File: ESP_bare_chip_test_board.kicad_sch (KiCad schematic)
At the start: 0 parts

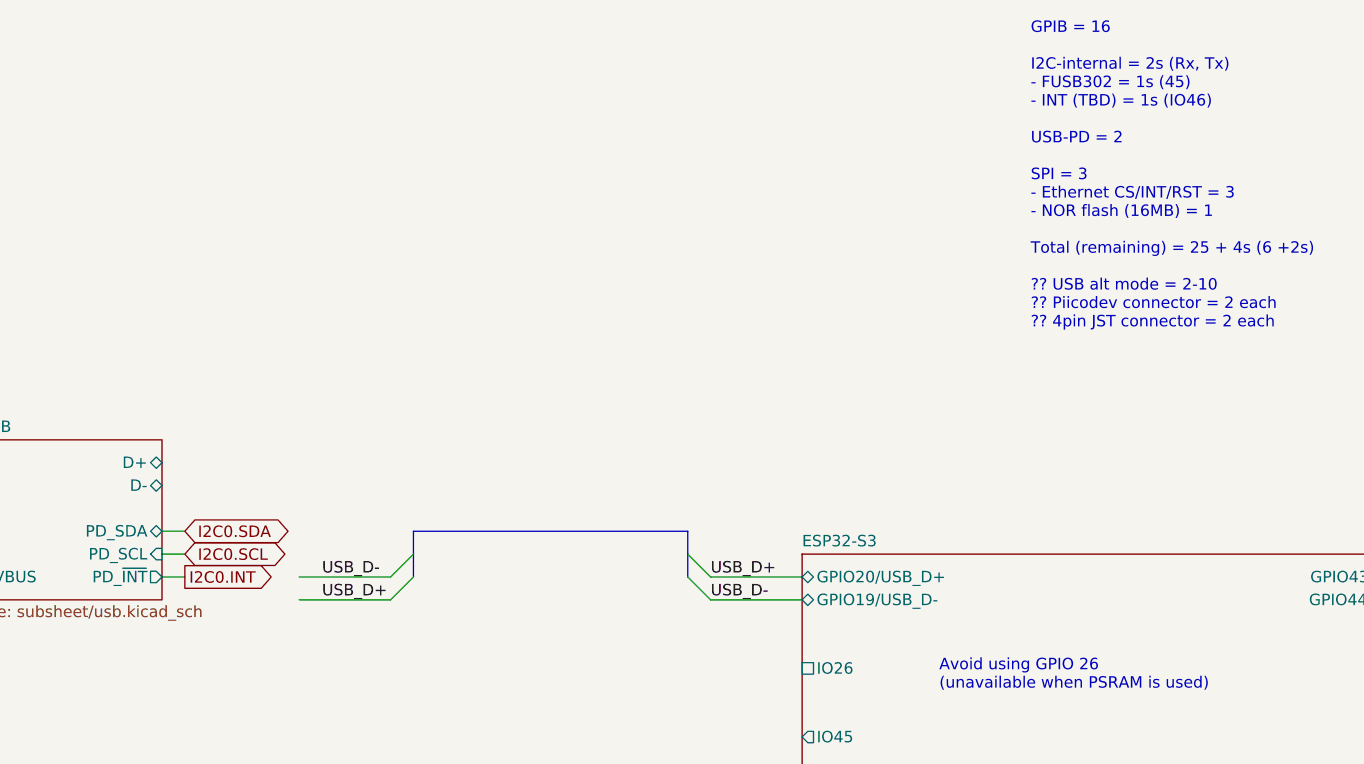
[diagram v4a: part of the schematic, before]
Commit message: Add barrel jack to schematic
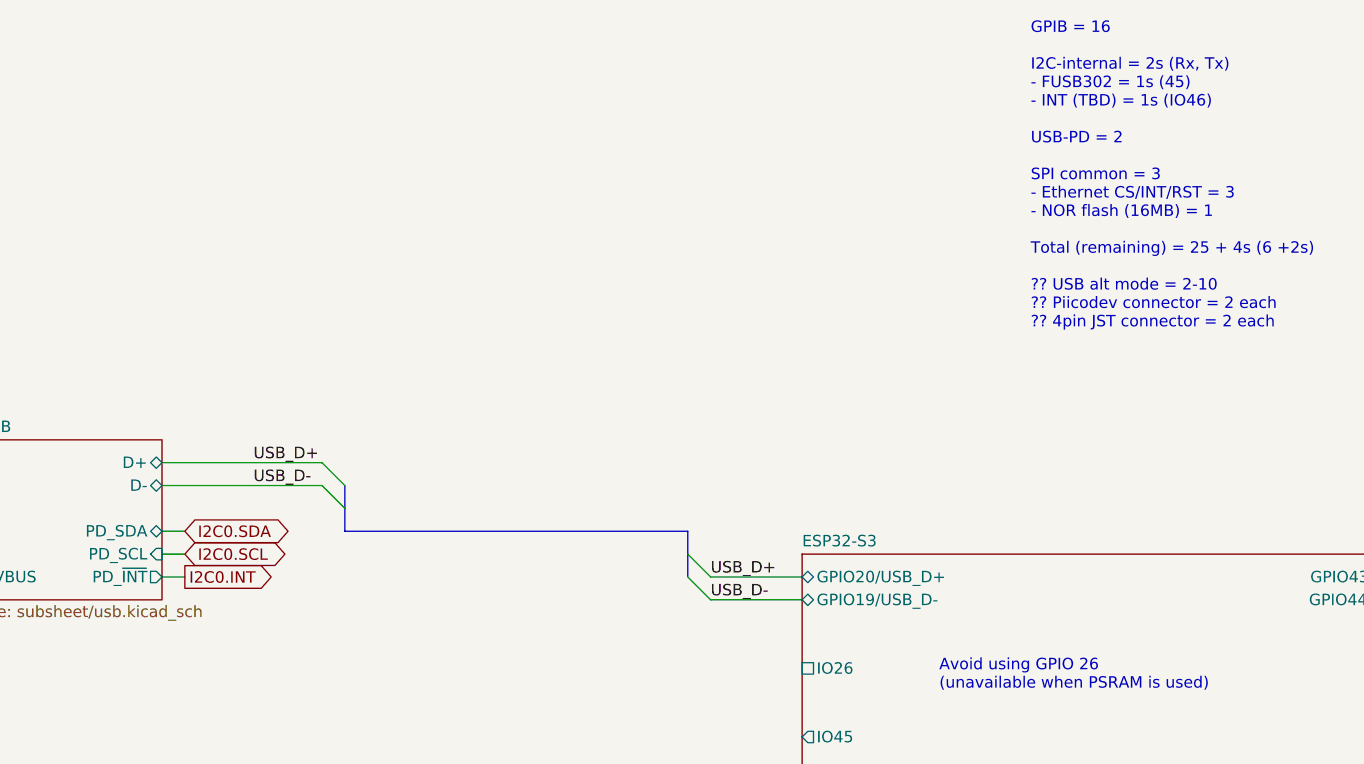
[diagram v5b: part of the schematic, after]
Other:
- note added: "~~ GPIO count ~~ Unrestricted = 31 Special = 6s (0, 45, 46, Tx, Rx) Unused if possible = 1u (26) GPIB = 16 I2C-internal = 2s (Rx, Tx) - FUSB302 = 1s (45) - INT (TBD) = 1s (IO46) USB-PD = 2 SPI common = 3 - Ethernet CS/INT/RST = 3 - NOR flash (16MB) = 1 Total (remaining) = 25 + 4s (6 +2s) ?? USB alt mode = 2-10 ?? Piicodev connector = 2 each ?? 4pin JST connector = 2 each"
- note removed: "~~ GPIO count ~~ Unrestricted = 31 Special = 6s (0, 45, 46, Tx, Rx) Unused if possible = 1u (26) GPIB = 16 I2C-internal = 2s (Rx, Tx) - FUSB302 = 1s (45) - INT (TBD) = 1s (IO46) USB-PD = 2 SPI = 3 - Ethernet CS/INT/RST = 3 - NOR flash (16MB) = 1 Total (remaining) = 25 + 4s (6 +2s) ?? USB alt mode = 2-10 ?? Piicodev connector = 2 each ?? 4pin JST connector = 2 each"
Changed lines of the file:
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@@
 	)
 	(bus_entry
-		(at 63.5 33.02)
-		(size 2.54 -2.54)
+		(at 55.88 22.86)
+		(size 2.54 2.54)
 		(stroke
 			(width 0)
@@
 	)
 	(bus_entry
-		(at 63.5 35.56)
-		(size 2.54 -2.54)
+		(at 55.88 20.32)
+		(size 2.54 2.54)
 		(stroke
 			(width 0)
@@
 	(wire
 		(pts
-			(xy 53.34 35.56) (xy 63.5 35.56)
-		)
-		(stroke
-			(width 0)
-			(type default)
-		)
-	)
-	(wire
-		(pts
 			(xy 17.78 33.02) (xy 15.24 33.02)
 		)
@@
 	(bus
 		(pts
-			(xy 66.04 30.48) (xy 66.04 27.94)
+			(xy 58.42 25.4) (xy 58.42 27.94)
 		)
 		(stroke
@@
 		)
 	)
+	(wire
+		(pts
+			(xy 38.1 22.86) (xy 55.88 22.86)
+		)
+		(stroke
+			(width 0)
+			(type default)
+		)
+	)
 	(bus
 		(pts
@@
 		)
 	)
+	(wire
+		(pts
+			(xy 88.9 91.44) (xy 88.9 121.92)
+		)
+		(stroke
+			(width 0)
+			(type default)
+		)
+	)
 	(bus
 		(pts
-			(xy 66.04 27.94) (xy 96.52 27.94)
-		)
-		(stroke
-			(width 0)
-			(type default)
-		)
-	)
-	(wire
-		(pts
-			(xy 88.9 91.44) (xy 88.9 121.92)
+			(xy 58.42 27.94) (xy 96.52 27.94)
 		)
 		(stroke
@@
 	(wire
 		(pts
+			(xy 38.1 20.32) (xy 55.88 20.32)
+		)
+		(stroke
+			(width 0)
+			(type default)
+		)
+	)
+	(wire
+		(pts
 			(xy 88.9 121.92) (xy 88.9 134.62)
 		)
@@
 	(wire
 		(pts
-			(xy 53.34 33.02) (xy 63.5 33.02)
-		)
-		(stroke
-			(width 0)
-			(type default)
-		)
-	)
-	(wire
-		(pts
 			(xy 99.06 35.56) (xy 109.22 35.56)
 		)
@@
 	(bus
 		(pts
-			(xy 66.04 33.02) (xy 66.04 30.48)
+			(xy 58.42 22.86) (xy 58.42 25.4)
 		)
 		(stroke
@@
 		)
 	)
-	(text "~~ GPIO count ~~\nUnrestricted = 31\nSpecial = 6s (0, 45, 46, Tx, Rx)\nUnused if possible = 1u (26)\n\nGPIB = 16\n\nI2C-internal = 2s (Rx, Tx)\n- FUSB302 = 1s (45)\n- INT (TBD) = 1s (IO46)\n\nUSB-PD = 2\n\nSPI = 3\n- Ethernet CS/INT/RST = 3\n- NOR flash (16MB) = 1\n\nTotal (remaining) = 25 + 4s (6 +2s)\n\n?? USB alt mode = 2-10\n?? Piicodev connector = 2 each\n?? 4pin JST connector = 2 each\n  "
+	(text "~~ GPIO count ~~\nUnrestricted = 31\nSpecial = 6s (0, 45, 46, Tx, Rx)\nUnused if possible = 1u (26)\n\nGPIB = 16\n\nI2C-internal = 2s (Rx, Tx)\n- FUSB302 = 1s (45)\n- INT (TBD) = 1s (IO46)\n\nUSB-PD = 2\n\nSPI common = 3\n- Ethernet CS/INT/RST = 3\n- NOR flash (16MB) = 1\n\nTotal (remaining) = 25 + 4s (6 +2s)\n\n?? USB alt mode = 2-10\n?? Piicodev connector = 2 each\n?? 4pin JST connector = 2 each\n  "
 		(exclude_from_sim no)
 		(at 134.62 7.62 0)
@@
 	)
 	(label "USB_D+"
-		(at 55.88 35.56 0)
+		(at 48.26 20.32 0)
 		(fields_autoplaced yes)
 		(effects
@@
 	)
 	(label "USB_D-"
-		(at 55.88 33.02 0)
-		(fields_autoplaced yes)
-		(effects
+		(at 48.26 22.86 0)
+		(fields_autoplaced yes)
+		(effects

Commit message: Uknown changes?File formats?
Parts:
- added R101: 0, Resistor_SMD:R_0402_1005Metric, symbol Device:R_US
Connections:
- net ESP32-C3/IO2/STRAP^{PU}: now also R101.2
- net ~{ETH_INT}: now also R101.1

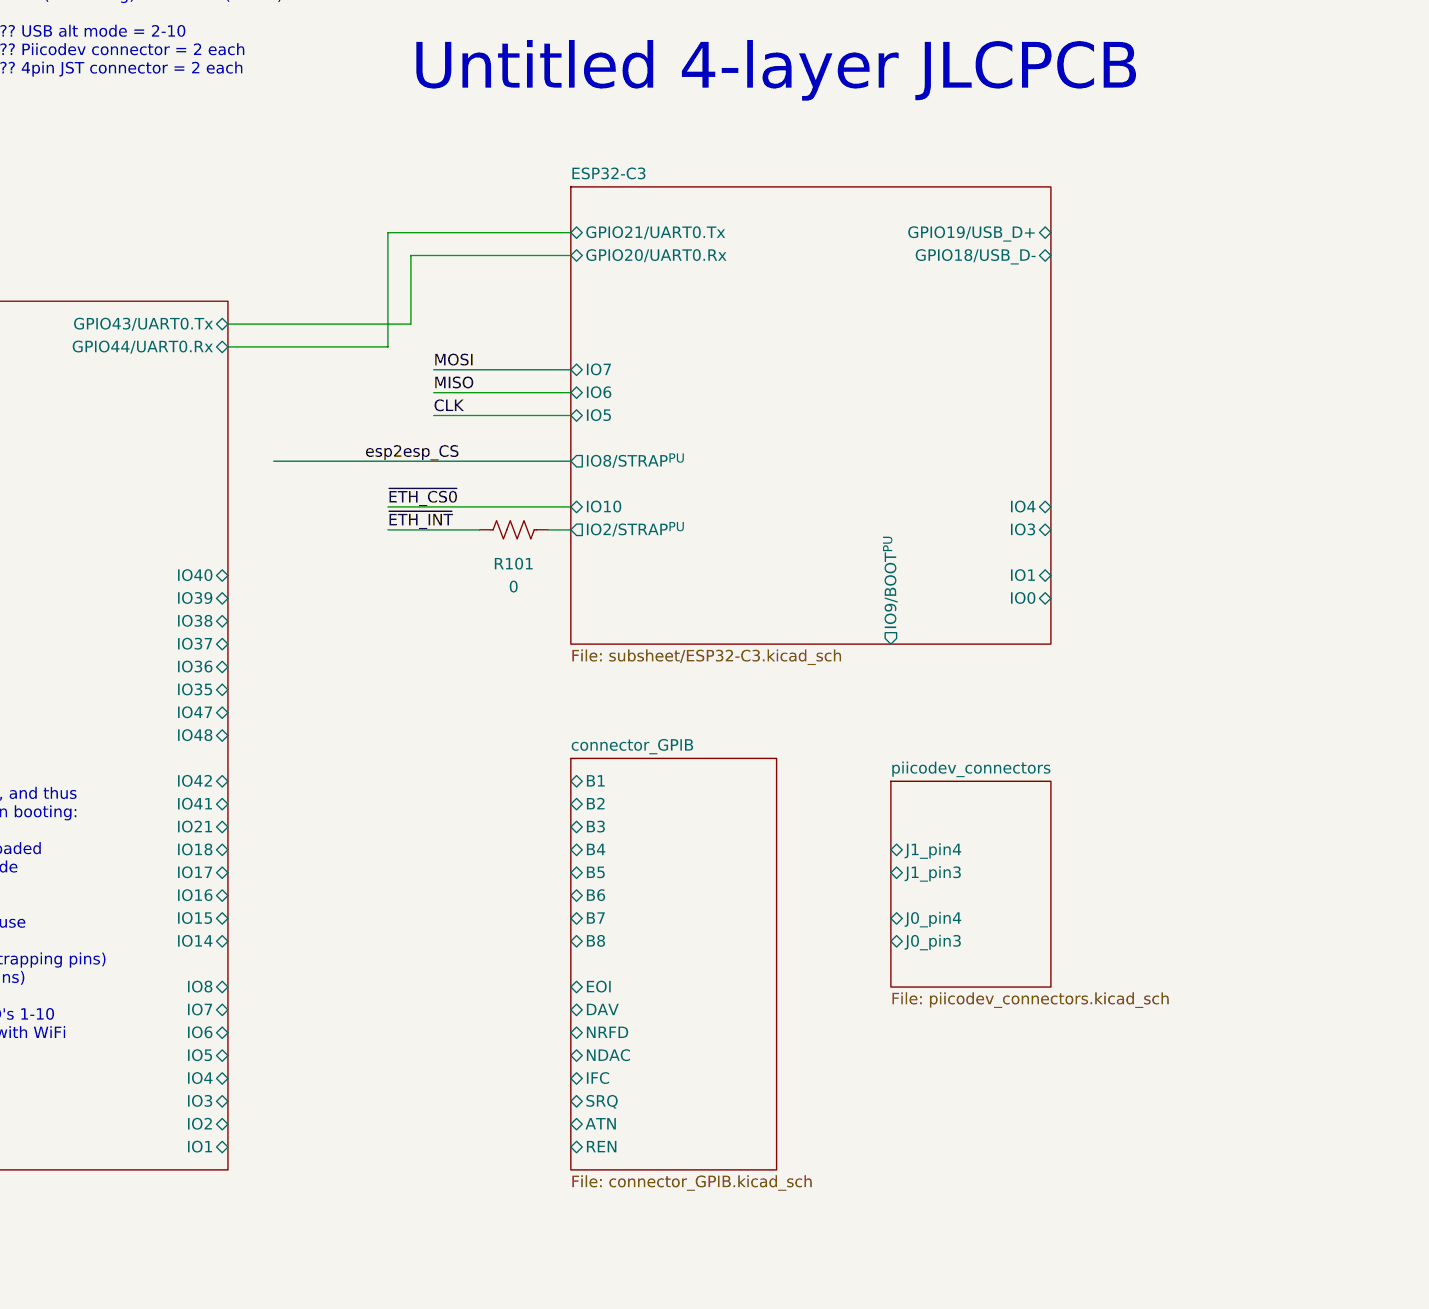
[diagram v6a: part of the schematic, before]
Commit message: Unknown changes? Arranging components, I believe
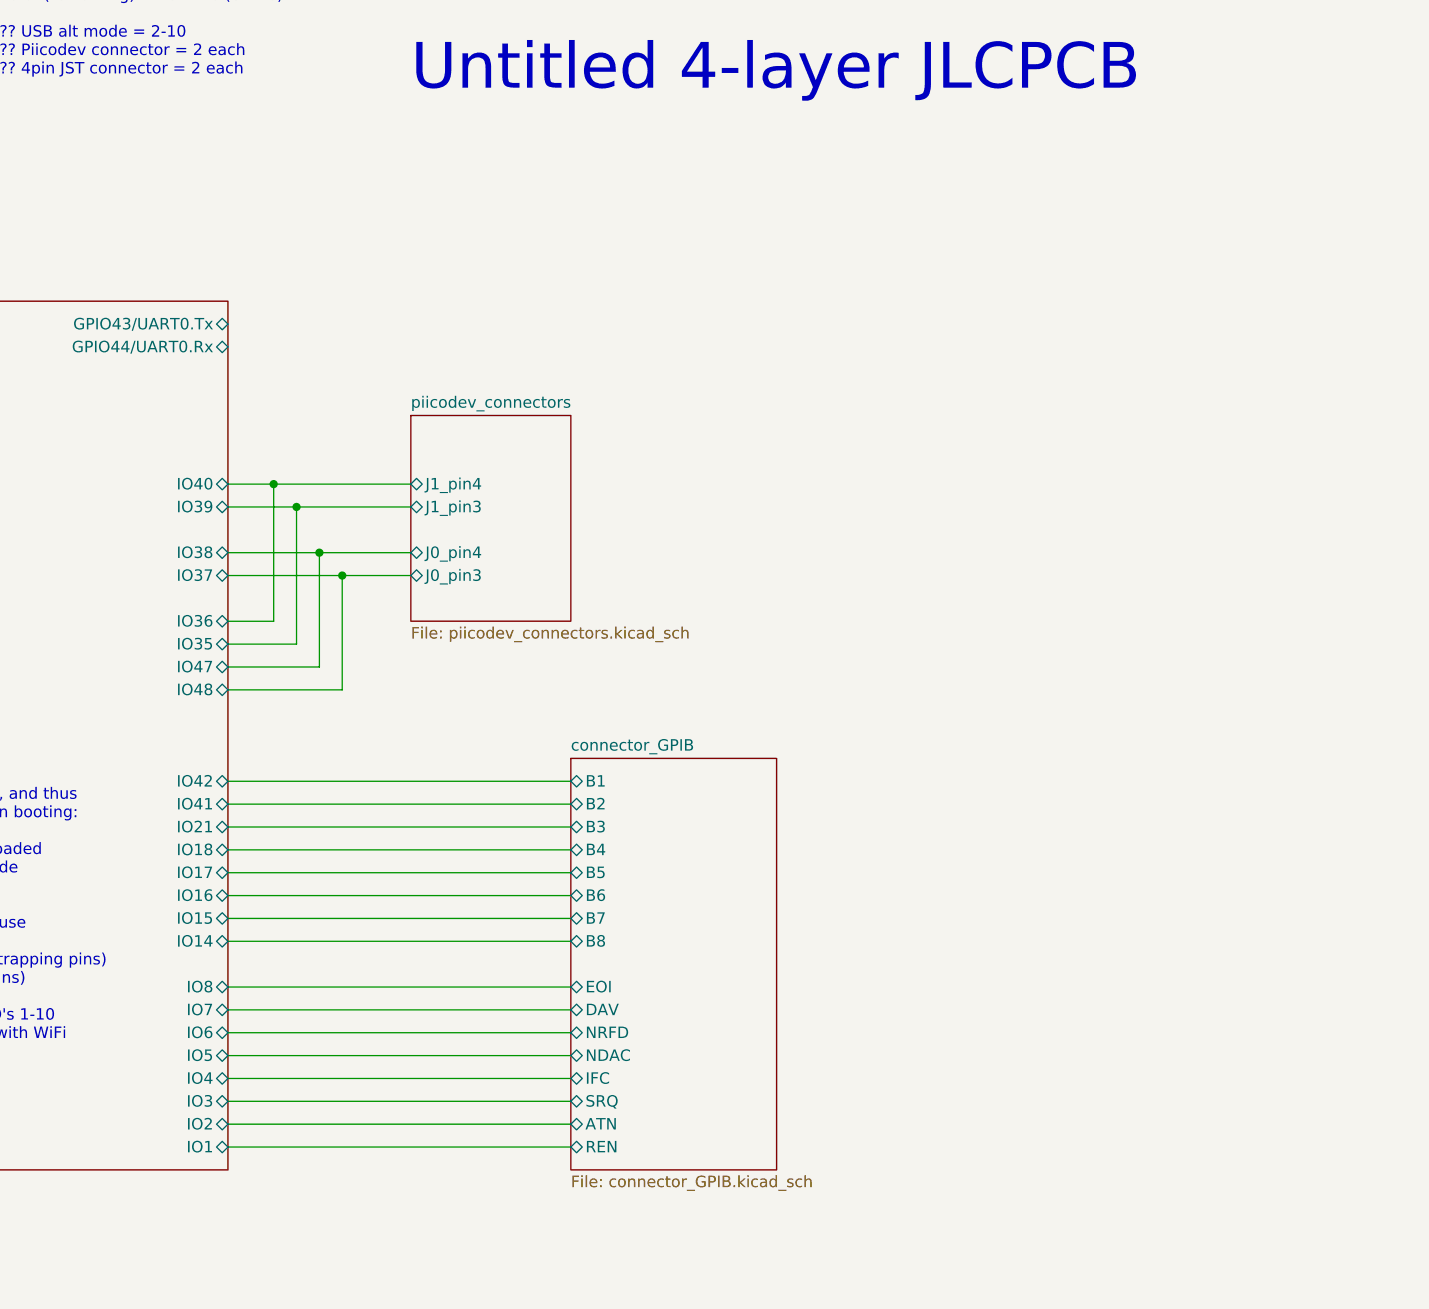
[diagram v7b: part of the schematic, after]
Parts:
- removed R101: 0, Resistor_SMD:R_0402_1005Metric, symbol Device:R_US
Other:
- removed sheet ESP32-C3
